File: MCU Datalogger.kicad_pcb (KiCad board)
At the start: 2 copper layers, 29 parts, among them J1 Conn_01x04_Male, J2 Conn_01x09_Male, J3 Conn_01x04_Male, J4 Conn_02x03_Odd_Even, U1 24LC1025, U2 DS1337S_, U3 24LC1025, U4 ATMEGA328P-AU, Y1 32.768 MHz, Y2 16 MHz

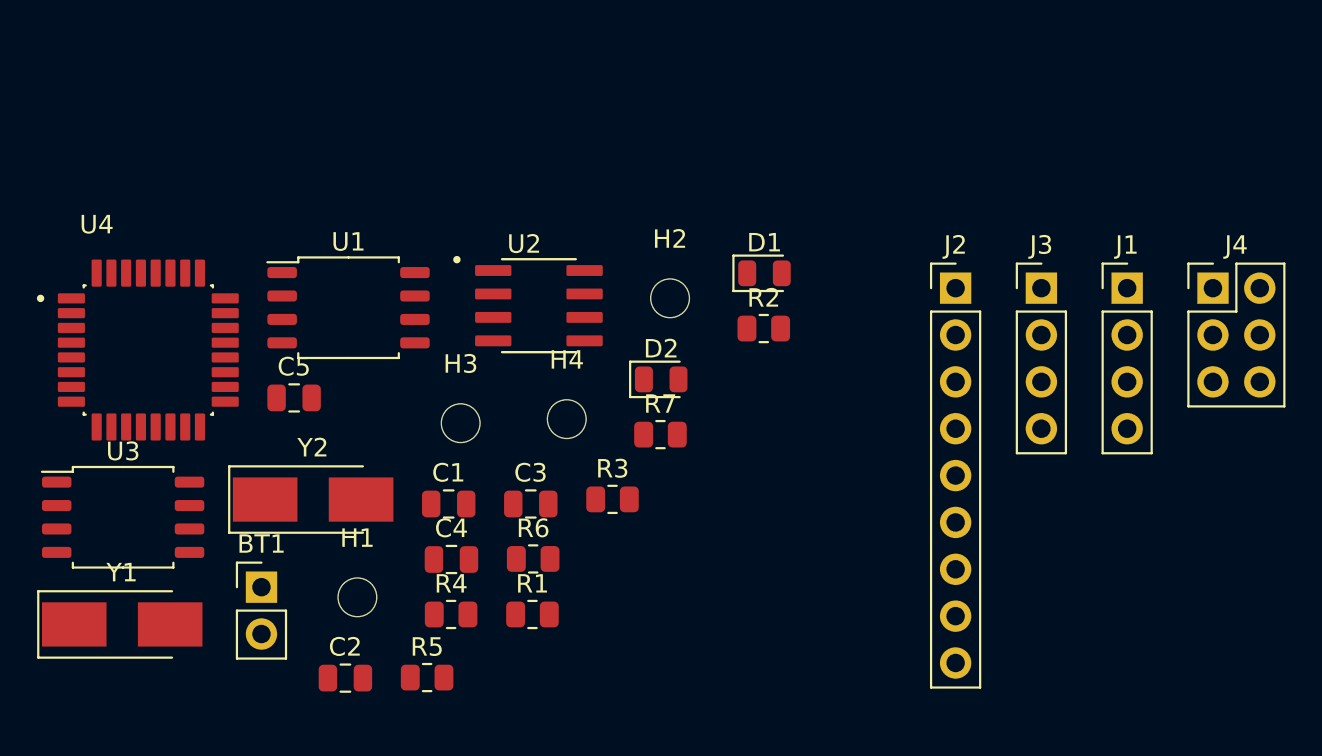
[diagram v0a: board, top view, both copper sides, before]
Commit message: Completed placement of footprints.
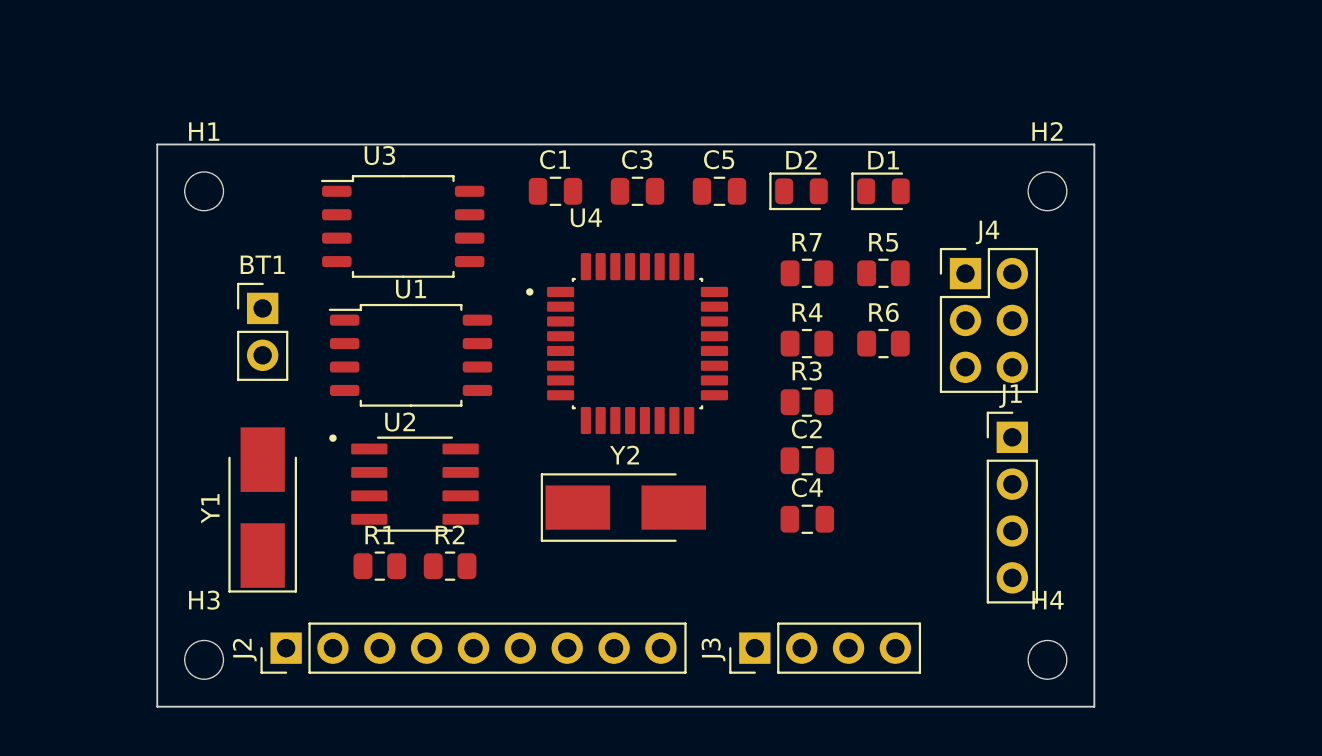
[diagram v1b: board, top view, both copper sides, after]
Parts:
- moved J2 41.2 mm to (126.4, 108.6), turned to 90 degrees
- moved R5 33.1 mm to (158.8, 88.3)
- moved H4 29.1 mm to (167.6, 109.2)
- moved C2 27.7 mm to (154.6, 98.4)
- moved U4 26.5 mm to (145.4, 92.1)
- moved C5 25.6 mm to (149.9, 83.8)
- moved J3 24.9 mm to (151.8, 108.6), turned to 90 degrees
- moved R4 24.2 mm to (154.6, 92.1)
- moved H1 23.5 mm to (121.9, 83.8)
- moved R6 22.3 mm to (158.8, 92.1)
- moved U3 21.9 mm to (132.7, 85.7)
- moved R2 21.3 mm to (135.3, 104.1)
- moved H2 21.3 mm to (167.6, 83.8)
- moved C4 19.4 mm to (154.6, 101.6)
- moved H3 18.9 mm to (121.9, 109.2)
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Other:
- board outline added: 50.8 x 30.5 mm

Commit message: Refined and completed outline
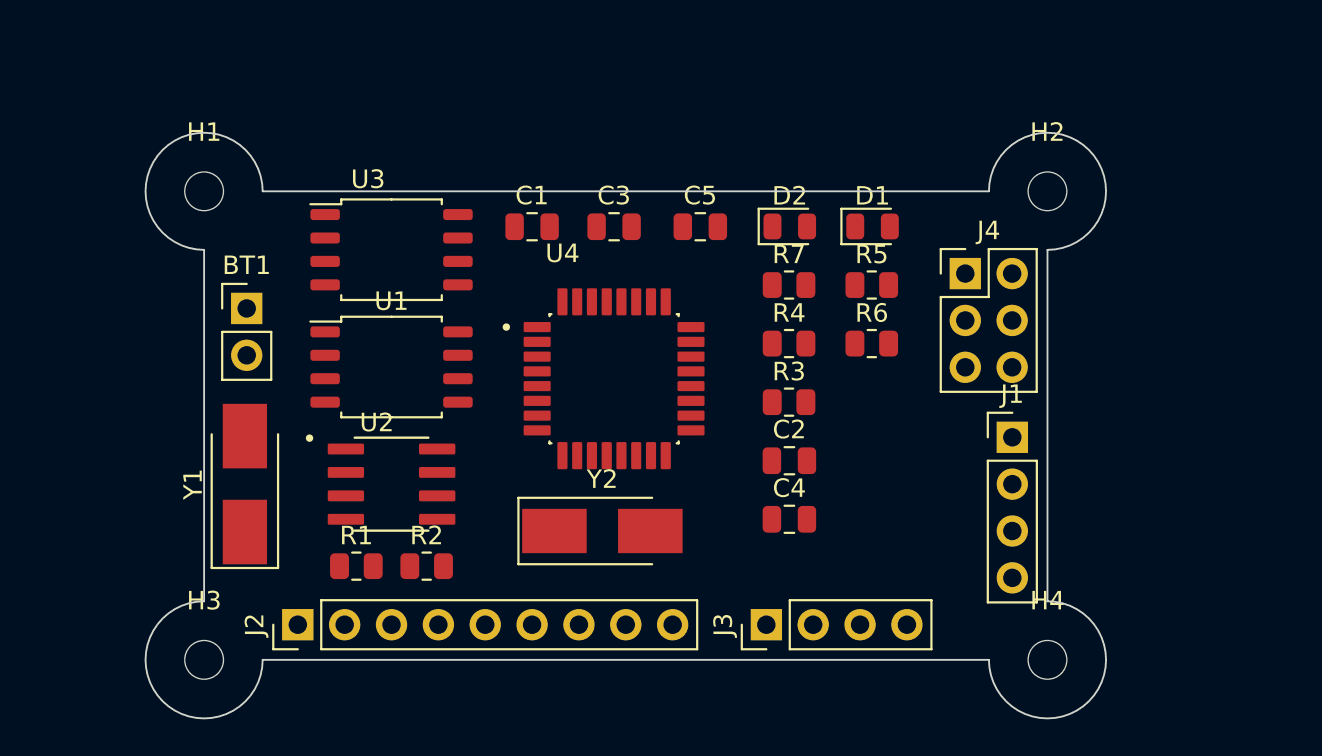
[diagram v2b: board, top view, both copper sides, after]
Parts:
- moved C1 2.30 mm to (139.7, 85.7)
- moved C3 2.30 mm to (144.1, 85.7)
- moved U4 2.29 mm to (144.1, 94.0)
- moved C5 2.18 mm to (148.8, 85.7)
- moved D2 2.01 mm to (153.7, 85.7)
- moved D1 2.00 mm to (158.2, 85.7)
- moved Y2 1.80 mm to (143.5, 102.2)
- moved Y1 1.60 mm to (124.1, 99.7)
- moved J2 1.42 mm to (127.0, 107.3)
- moved J3 1.42 mm to (152.4, 107.3)
- moved U3 1.41 mm to (132.1, 87.0)
- moved R1 1.27 mm to (130.2, 104.1)
- moved R2 1.27 mm to (134.0, 104.1)
- moved U2 1.27 mm to (132.1, 99.7)
- moved U1 1.24 mm to (132.1, 93.3)
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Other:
- board size 50.8 x 30.5 mm -> 52.1 x 31.7 mm

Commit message: Routing sans GND Vcc complete.
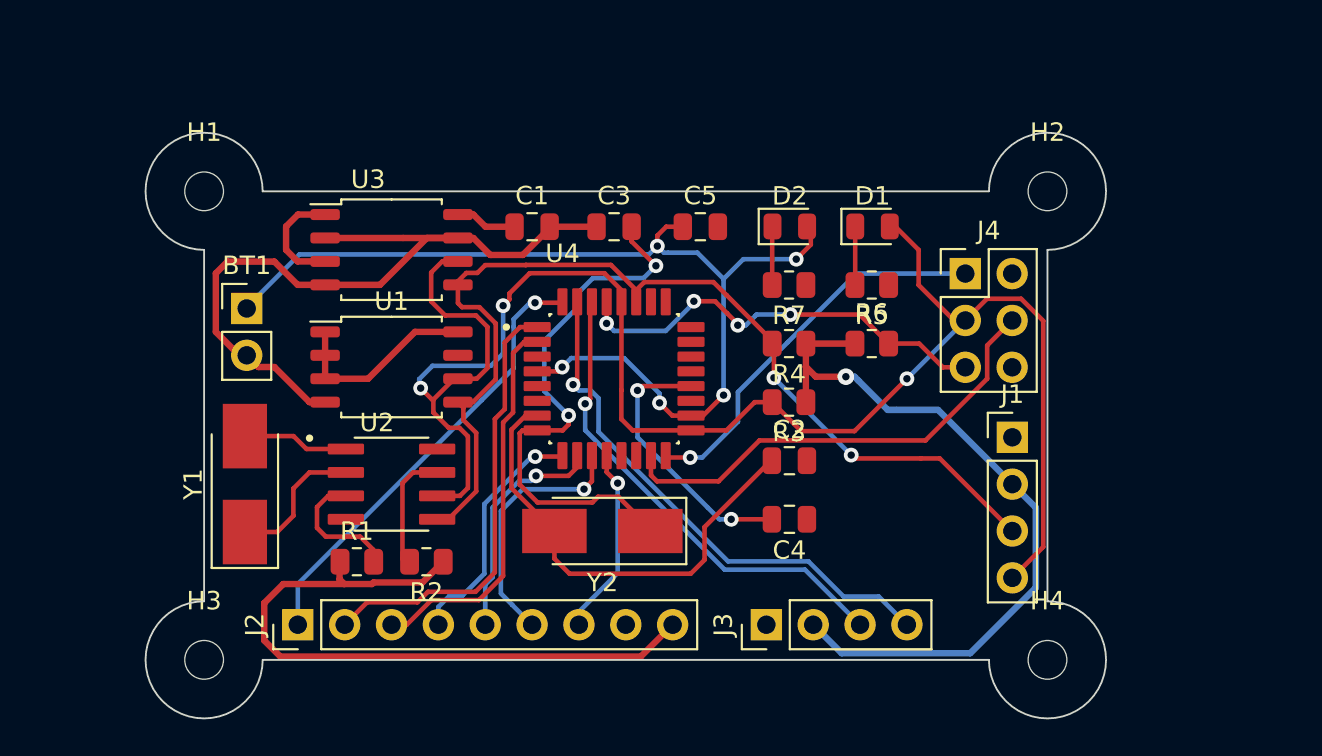
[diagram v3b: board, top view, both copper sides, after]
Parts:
- moved R1 0.24 mm to (130.2, 103.9)
- moved R2 0.24 mm to (134.0, 103.9), turned to 180 degrees
- turned C4 to 180 degrees
- turned R3 to 180 degrees
- turned R4 to 180 degrees
- turned R5 to 180 degrees
- turned R7 to 180 degrees
- turned Y2 to 180 degrees
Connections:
- C1 pad 1: Net-(C1-Pad1) -> /Vcc
- R1 pad 1: Net-(C1-Pad1) -> /Vcc
- R2 pad 1: Net-(C1-Pad1) -> /Vcc
- U1 pad 4: Net-(U1-Pad4) -> GND
- U1 pad 7: Net-(U1-Pad4) -> GND
- U2 pad 8: Net-(C1-Pad1) -> /Vcc
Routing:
- net /Vcc: track 0.00 -> 97.1 mm, vias 0 -> 1
- net /SCK: track 0.00 -> 94.2 mm, vias 0 -> 3
- net /SDA: track 0.00 -> 55.8 mm, vias 0 -> 2
- net Net-(BT1-Pad1): track 0.00 -> 55.5 mm, vias 0 -> 5
- net GND: track 0.00 -> 41.4 mm
- net Net-(C3-Pad2): track 0.00 -> 30.0 mm, vias 0 -> 2
- net /TX: track 0.00 -> 29.1 mm, vias 0 -> 1
- net /RX: track 0.00 -> 26.4 mm, vias 0 -> 1
- net /MOSI: track 0.00 -> 25.4 mm
- net Net-(C2-Pad1): track 0.00 -> 25.4 mm
- net /D2: track 0.00 -> 24.4 mm, vias 0 -> 1
- net /D3: track 0.00 -> 24.1 mm
- net /RESET: track 0.00 -> 23.5 mm, vias 0 -> 4
- net /MIS0: track 0.00 -> 21.4 mm, vias 0 -> 1
- net /D4: track 0.00 -> 21.0 mm
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
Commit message: Completed routing.
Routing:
- net GND: track 41.4 -> 142.6 mm, vias 0 -> 6
- net /Vcc: track 97.1 -> 149.3 mm, vias 1 -> 5
- net /RESET: track 23.5 -> 26.7 mm
- net /SCK: track 94.2 -> 96.1 mm
- net /SDA: track 55.8 -> 57.5 mm
- net /TX: track 29.1 -> 30.8 mm
- net Net-(U2-Pad7): track 6.79 -> 7.78 mm
- net /D2: track 24.4 -> 25.4 mm
- net /RX: track 26.4 -> 27.1 mm
- net /MOSI: track 25.4 -> 26.1 mm
- net /D4: track 21.0 -> 21.5 mm
- added copper zone on F.Cu, net /Vcc
- added copper zone on B.Cu, net GND

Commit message: Fixed outstanding issues.
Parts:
- added REF**: KiCad-Logo2_6mm_SilkScreen, Symbol:KiCad-Logo2_6mm_SilkScreen, B.Cu at (154.1, 88.2)
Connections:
- BT1 pad 1: Net-(BT1-Pad1) -> /Vcc
- C5 pad 1: Net-(BT1-Pad1) -> /Vcc
- D2 pad 2: Net-(BT1-Pad1) -> /Vcc
- U4 pad 18: Net-(BT1-Pad1) -> /Vcc
- U4 pad 4: Net-(BT1-Pad1) -> /Vcc
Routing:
- net Net-(BT1-Pad1): track 55.5 -> 0.00 mm, vias 5 -> 0
- net /Vcc: track 149.3 -> 204.7 mm, vias 5 -> 10
- net GND: track 142.6 -> 151.7 mm
- net /RESET: track 26.7 -> 25.5 mm
- net Net-(C3-Pad2): track 30.0 -> 29.0 mm
- net Net-(C2-Pad1): track 25.4 -> 26.1 mm
- net /MIS0: track 21.5 -> 21.0 mm
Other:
- board text added: "- 2Mbit EEPROM - RTC - I2C, SPI, GPIOS"
- board text added: "2"
- board text added: "3"
- board text added: "4"
- board text added: "5"
- board text added: "6"
- board text added: "7"
- board text added: "8"
- board text added: "Data logger with the ATMega"
- board text added: "GND"
- board text added: "GPIO"
- board text added: "I2C"
- board text added: "ICSP"
- board text added: "ICSP MISO | VCC SCK | MOSI RESET | GND"
- board text added: "RX"
- board text added: "Serial"
- board text added: "TX"
- board text added: "VCC"
- board text added: "by Taulant Shala"
